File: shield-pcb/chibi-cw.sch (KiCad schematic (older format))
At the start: 56 parts, among them J1 HEADPHONES, K1 CONN_3, K2 CONN_3, P1 CONN_4, P2 CONN_4, P3 CONN_2, Q1 BC847, U1 TPA6130A2

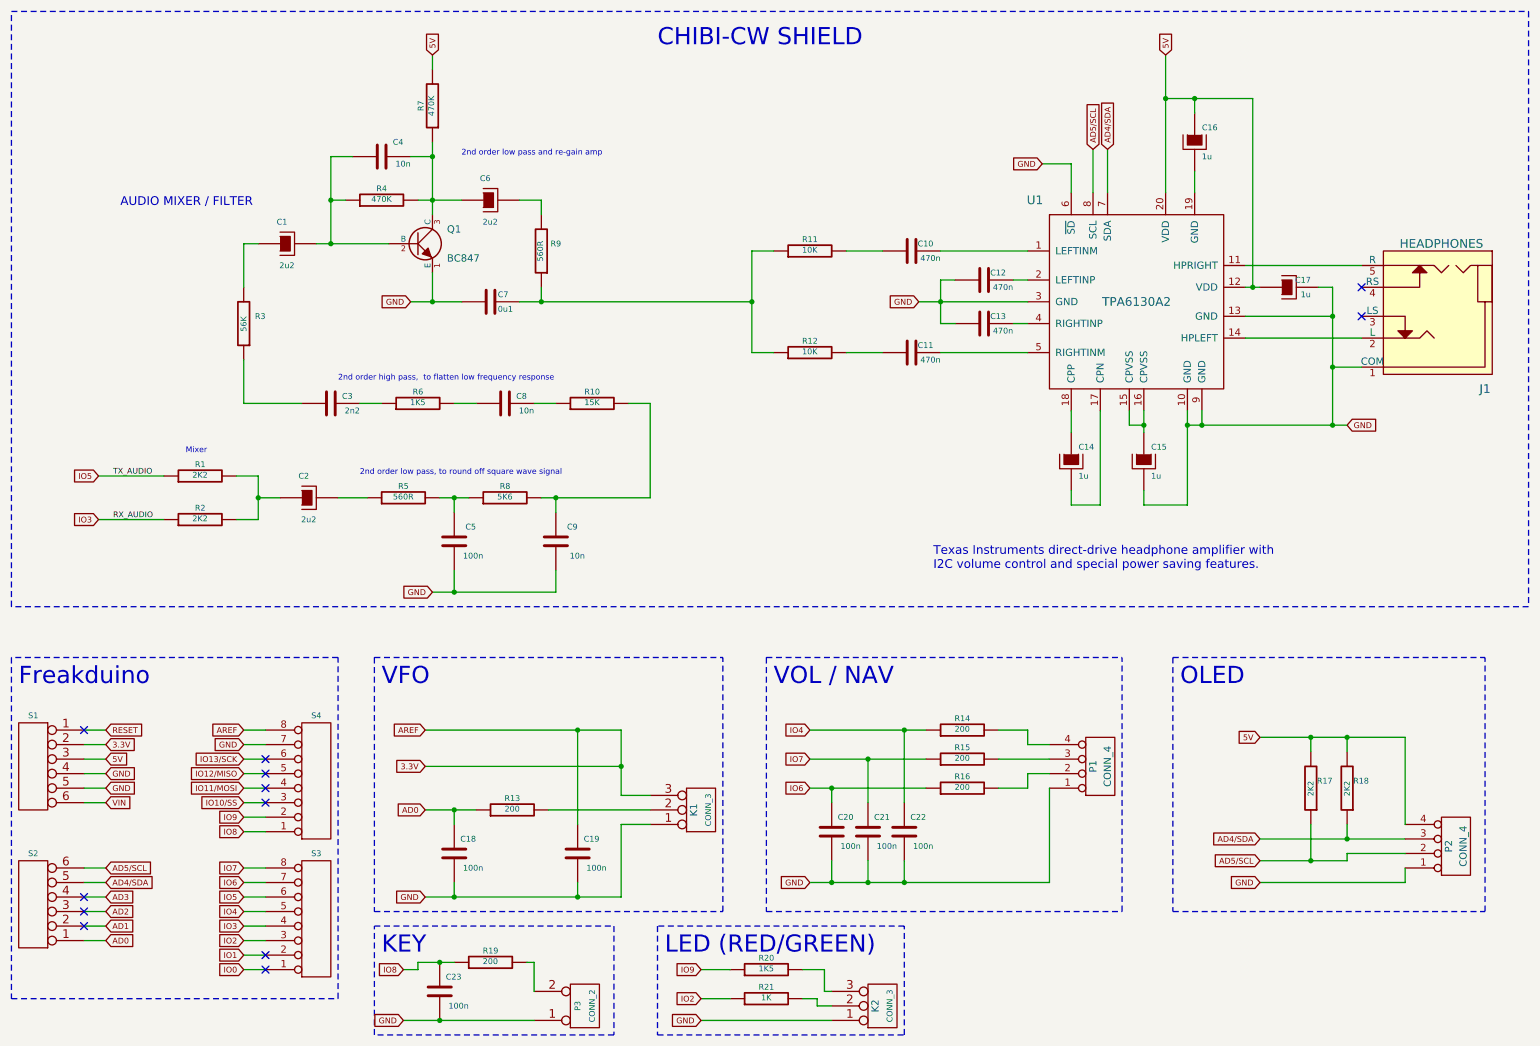
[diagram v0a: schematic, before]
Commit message: 3D connector parts improved (more accurate size etc)
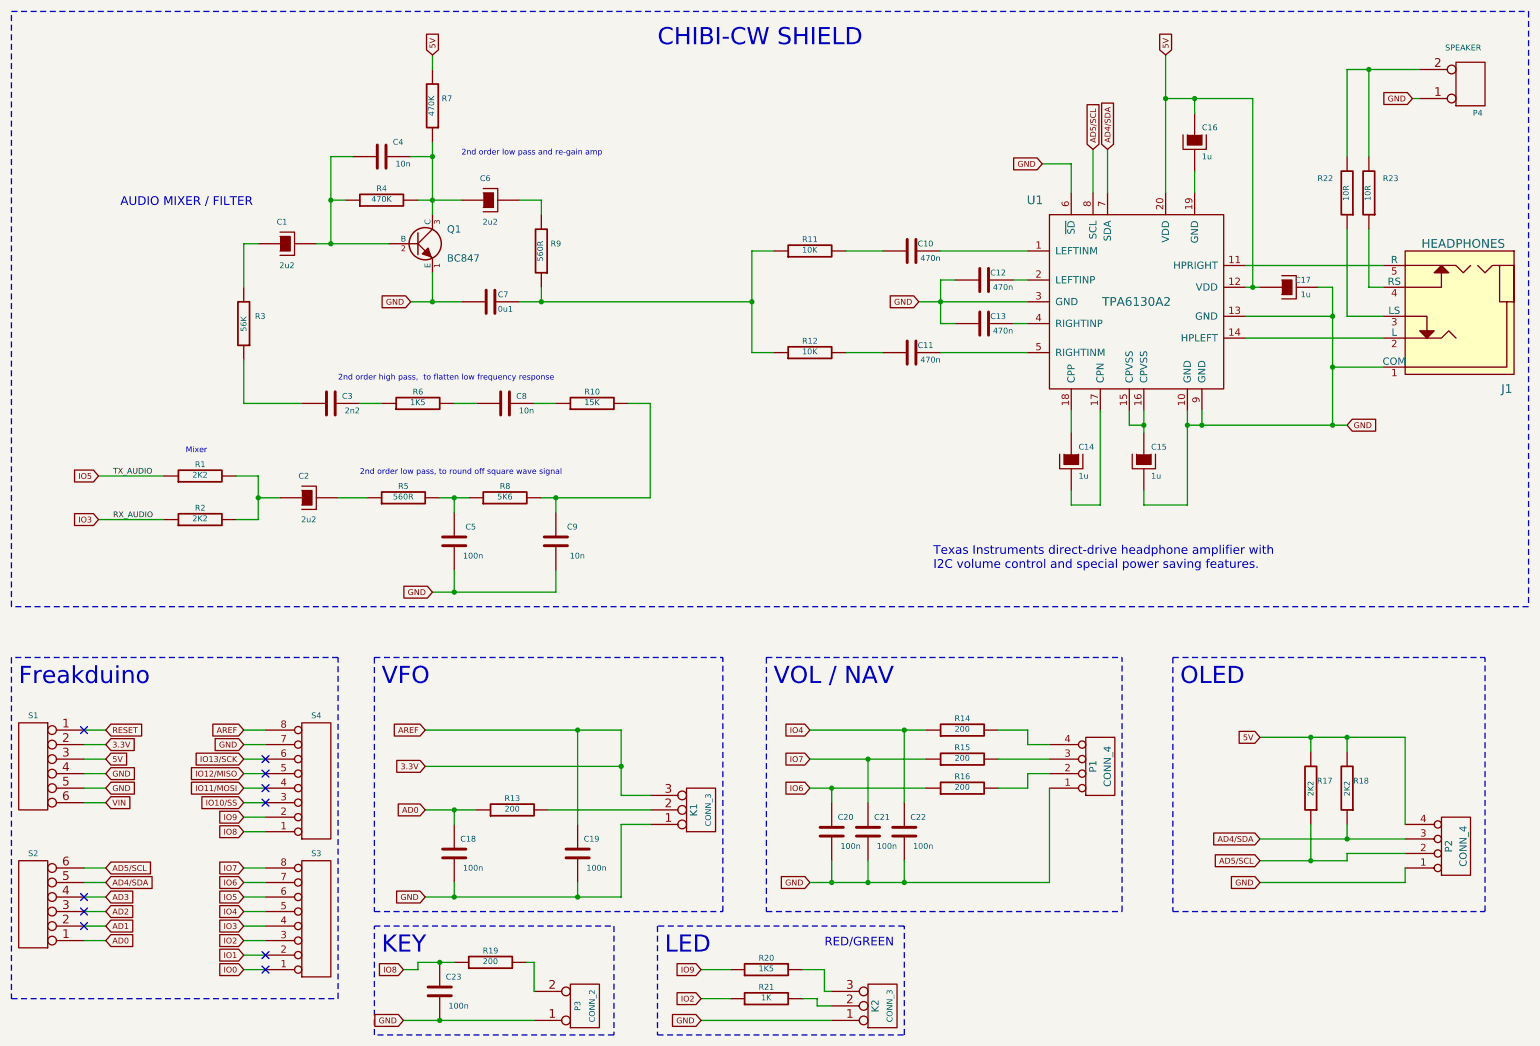
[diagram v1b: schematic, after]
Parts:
- added P4: SPEAKER, symbol CONN_2
- added R22, R23: 10R, ~, symbol R
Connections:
- net GND: now also P4.1 (P1)
- net at J1.3 (LS): now also R22.1
- net at J1.4 (RS): now also R23.1
- new net: P4.2 (PM), R22.2, R23.2
- no-connect marks 12 -> 10
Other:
- note added: "LED"
- note added: "RED/GREEN"
- note removed: "LED (RED/GREEN)"
- moved on the sheet: J1
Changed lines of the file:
@@
 Sheet 1 1
 Title "CHIBI-CW 2.4GHz Transceiver Freakduino Shield"
-Date "4 aug 2013"
+Date "5 aug 2013"
 Rev "v1.0"
 Comp ""
@@
 L AUDIO_ST_DPST J1
 U 1 1 51F8E415
-P 10200 2700
-F 0 "J1" H 9650 2150 60  0000 C CNN
-F 1 "HEADPHONES" H 9950 3150 60  0000 C CNN
-F 2 "~" H 10250 2450 60  0000 C CNN
-F 3 "~" H 10250 2450 60  0000 C CNN
-	1    10200 2700
+P 10350 2700
+F 0 "J1" H 9800 2150 60  0000 C CNN
+F 1 "HEADPHONES" H 10100 3150 60  0000 C CNN
+F 2 "~" H 10400 2450 60  0000 C CNN
+F 3 "~" H 10400 2450 60  0000 C CNN
+	1    10350 2700
 	-1   0    0    -1
 $EndComp
@@
 U 1 1 51FCA9C4
 P 3500 1300
-F 0 "R7" V 3580 1300 40  0000 C CNN
+F 0 "R7" H 3400 1250 40  0000 C CNN
 F 1 "470K" V 3507 1301 40  0000 C CNN
 F 2 "~" V 3430 1300 30  0000 C CNN
@@
 19 27 0E 00 BA BA BA C6 9C FA 7E 5C FC EF D1 B8 4F 18 9F 5D E2 3E A7 65 A5 F1 63 82 B8 31 E2 73
 BD E6 30 1E 4C 68 DC 18 31 41 DC 18 F1 FF 01 FB E6 BD DE C7 35 91 78 00 00 00 00 49 45 4E 44 AE
-42 60 82 B6 $EndBitmap
+42 60 82 0A $EndBitmap
 EndData
 $EndBitmap
@@
 	8400 3950 8400 4050
 Wire Wire Line
-	9100 2400 9900 2400
-Wire Wire Line
-	9900 2900 9100 2900
-Wire Wire Line
-	9700 3100 9900 3100
+	9100 2400 10050 2400
+Wire Wire Line
+	10050 2900 9100 2900
+Wire Wire Line
+	9700 3100 10050 3100
 Wire Wire Line
 	8750 1250 8750 1350
@@
 Wire Notes Line
 	8600 5100 10750 5100
-NoConn ~ 9900 2550
-NoConn ~ 9900 2750
 NoConn ~ 1100 6950
 NoConn ~ 1100 6850
@@
 	5350 7600 6250 7600
 Text Notes 5100 7150 0    118  ~ 0
-LED (RED/GREEN)
+LED
 $Comp
 L CONN_3 K2
@@
 Wire Wire Line
 	3400 7250 3300 7250
+Text Notes 6200 7100 0    59   ~ 0
+RED/GREEN
+$Comp
+L CONN_2 P4
+U 1 1 51FEF6DB
+P 10650 1150
+F 0 "P4" H 10700 1350 40  0000 C CNN
+F 1 "SPEAKER" H 10600 900 40  0000 C CNN
+F 2 "" H 10650 1150 60  0000 C CNN
+F 3 "" H 10650 1150 60  0000 C CNN
+	1    10650 1150
+	1    0    0    1
+$EndComp
+Wire Wire Line
+	10050 2550 9950 2550
+Wire Wire Line
+	9950 2550 9950 2150
+Wire Wire Line
+	10050 2750 9800 2750
+Wire Wire Line
+	9800 2750 9800 2150
+$Comp
+L R R22
+U 1 1 51FEFADD
+P 9800 1900
+F 0 "R22" H 9950 1800 40  0000 C CNN
+F 1 "10R" V 9807 1901 40  0000 C CNN
+F 2 "~" V 9730 1900 30  0000 C CNN
+F 3 "~" H 9800 1900 30  0000 C CNN
+	1    9800 1900
+	-1   0    0    1
+$EndComp
+$Comp
+L R R23
+U 1 1 51FEFAE3
+P 9950 1900
+F 0 "R23" H 9800 1800 40  0000 C CNN
+F 1 "10R" V 9957 1901 40  0000 C CNN
+F 2 "~" V 9880 1900 30  0000 C CNN
+F 3 "~" H 9950 1900 30  0000 C CNN
+	1    9950 1900
+	-1   0    0    1
+$EndComp
+Wire Wire Line
+	9800 1650 9800 1050
+Wire Wire Line
+	9800 1050 10300 1050
+Wire Wire Line
+	9950 1650 9950 1050
+Connection ~ 9950 1050
+Text GLabel 10250 1250 0    40   Input ~ 0
+GND
+Wire Wire Line
+	10250 1250 10300 1250
 $EndSCHEMATC
